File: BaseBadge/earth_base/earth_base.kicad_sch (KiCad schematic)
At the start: 8 parts, among them J1 Conn_02x03_Counter_Clockwise, J2 Conn_02x03_Counter_Clockwise

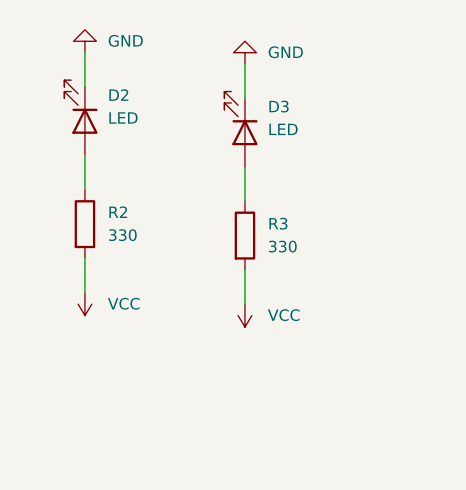
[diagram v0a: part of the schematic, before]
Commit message: overhauls across boards to v02
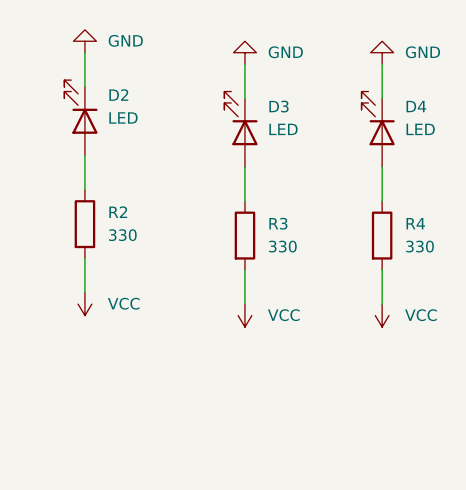
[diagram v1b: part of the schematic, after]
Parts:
- added D4: LED, LED_SMD:LED_1206_3216Metric_Pad1.42x1.75mm_HandSolder, symbol Device:LED
- added R4: 330, Resistor_SMD:R_1206_3216Metric, symbol Device:R
- D1, D2, D3: footprint (none) -> LED_SMD:LED_1206_3216Metric_Pad1.42x1.75mm_HandSolder
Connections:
- net GND: now also D4.1 (K)
- net VCC: now also R4.2
- new net: D4.2 (A), R4.1
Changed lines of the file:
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@@
+    (stroke (width 0) (type default) (color 0 0 0 0))
+  )
+  (wire (pts (xy 208.28 64.77) (xy 208.28 68.58))
     (stroke (width 0) (type default) (color 0 0 0 0))
   )
@@
     (stroke (width 0) (type default) (color 0 0 0 0))
   )
+  (wire (pts (xy 208.28 76.2) (xy 208.28 80.01))
+    (stroke (width 0) (type default) (color 0 0 0 0))
+  )
   (wire (pts (xy 128.27 143.51) (xy 163.83 143.51))
     (stroke (width 0) (type default) (color 0 0 0 0))
@@
     (stroke (width 0) (type default) (color 0 0 0 0))
   )
+  (wire (pts (xy 208.28 87.63) (xy 208.28 91.44))
+    (stroke (width 0) (type default) (color 0 0 0 0))
+  )
   (wire (pts (xy 128.27 127) (xy 128.27 143.51))
     (stroke (width 0) (type default) (color 0 0 0 0))
@@
   (wire (pts (xy 123.19 132.08) (xy 123.19 138.43))
     (stroke (width 0) (type default) (color 0 0 0 0))
+  )
+  (symbol (lib_id "power:VCC") (at 208.28 91.44 180) (unit 1)
+    (in_bom yes) (on_board yes) (fields_autoplaced)
+    (property "Reference" "#PWR012" (id 0) (at 208.28 87.63 0)
+      (effects (font (size 1.27 1.27)) hide)
+    )
+    (property "Value" "VCC" (id 1) (at 210.82 92.7099 0)
+      (effects (font (size 1.27 1.27)) (justify right))
+    )
+    (property "Footprint" "" (id 2) (at 208.28 91.44 0)
+      (effects (font (size 1.27 1.27)) hide)
+    )
+    (property "Datasheet" "" (id 3) (at 208.28 91.44 0)
+      (effects (font (size 1.27 1.27)) hide)
+    )
+    (pin "1")
   )
   (symbol (lib_id "power:PWR_FLAG") (at 110.49 127 0) (unit 1)
@@
       (effects (font (size 1.27 1.27)) (justify left))
     )
-    (property "Footprint" "" (id 2) (at 175.26 71.12 0)
+    (property "Footprint" "LED_SMD:LED_1206_3216Metric_Pad1.42x1.75mm_HandSolder" (id 2) (at 175.26 71.12 0)
       (effects (font (size 1.27 1.27)) hide)
     )
@@
     )
     (pin "1")
+  )
+  (symbol (lib_id "Device:LED") (at 208.28 72.39 270) (unit 1)
+    (in_bom yes) (on_board yes)
+    (property "Reference" "D4" (id 0) (at 210.82 69.5324 90)
+      (effects (font (size 1.27 1.27)) (justify left))
+    )
+    (property "Value" "LED" (id 1) (at 210.82 72.0724 90)
+      (effects (font (size 1.27 1.27)) (justify left))
+    )
+    (property "Footprint" "LED_SMD:LED_1206_3216Metric_Pad1.42x1.75mm_HandSolder" (id 2) (at 208.28 72.39 0)
+      (effects (font (size 1.27 1.27)) hide)
+    )
+    (property "Datasheet" "~" (id 3) (at 208.28 72.39 0)
+      (effects (font (size 1.27 1.27)) hide)
+    )
+    (pin "1")
+    (pin "2")
   )
   (symbol (lib_id "power:PWR_FLAG") (at 146.05 127 0) (unit 1)
@@
     )
     (pin "1")
+  )
+  (symbol (lib_id "Device:R") (at 208.28 83.82 0) (unit 1)
+    (in_bom yes) (on_board yes) (fields_autoplaced)
+    (property "Reference" "R4" (id 0) (at 210.82 82.5499 0)
+      (effects (font (size 1.27 1.27)) (justify left))
+    )
+    (property "Value" "330" (id 1) (at 210.82 85.0899 0)
+      (effects (font (size 1.27 1.27)) (justify left))
+    )
+    (property "Footprint" "Resistor_SMD:R_1206_3216Metric" (id 2) (at 206.502 83.82 90)
+      (effects (font (size 1.27 1.27)) hide)
+    )
+    (property "Datasheet" "~" (id 3) (at 208.28 83.82 0)
+      (effects (font (size 1.27 1.27)) hide)
+    )
+    (pin "1")
+    (pin "2")
   )
   (symbol (lib_id "power:GND") (at 193.04 64.77 180) (unit 1)
@@
       (effects (font (size 1.27 1.27)) (justify left))
     )
-    (property "Footprint" "" (id 2) (at 158.75 69.85 0)
+    (property "Footprint" "LED_SMD:LED_1206_3216Metric_Pad1.42x1.75mm_HandSolder" (id 2) (at 158.75 69.85 0)
       (effects (font (size 1.27 1.27)) hide)
     )
@@
       (effects (font (size 1.27 1.27)) (justify left))
     )
-    (property "Footprint" "" (id 2) (at 193.04 72.39 0)
+    (property "Footprint" "LED_SMD:LED_1206_3216Metric_Pad1.42x1.75mm_HandSolder" (id 2) (at 193.04 72.39 0)
       (effects (font (size 1.27 1.27)) hide)
     )
@@
     (pin "1")
     (pin "2")
+  )
+  (symbol (lib_id "power:GND") (at 208.28 64.77 180) (unit 1)
+    (in_bom yes) (on_board yes) (fields_autoplaced)
+    (property "Reference" "#PWR011" (id 0) (at 208.28 58.42 0)
+      (effects (font (size 1.27 1.27)) hide)
+    )
+    (property "Value" "GND" (id 1) (at 210.82 63.4999 0)
+      (effects (font (size 1.27 1.27)) (justify right))
+    )
+    (property "Footprint" "" (id 2) (at 208.28 64.77 0)
+      (effects (font (size 1.27 1.27)) hide)
+    )
+    (property "Datasheet" "" (id 3) (at 208.28 64.77 0)
+      (effects (font (size 1.27 1.27)) hide)
+    )
+    (pin "1")
   )
   (symbol (lib_id "power:VCC") (at 175.26 90.17 180) (unit 1)
@@
       (reference "#PWR010") (unit 1) (value "VCC") (footprint "")
     )
+    (path "/7d7486ae-aeaa-4bbe-ab12-2142f8812c98"
+      (reference "#PWR011") (unit 1) (value "GND") (footprint "")
+    )
+    (path "/00fd3b26-9e35-452b-b74a-ccc9e0f65386"
+      (reference "#PWR012") (unit 1) (value "VCC") (footprint "")
+    )
     (path "/6ad5c8e3-405d-4457-b239-10abb6e3be61"
       (reference "D1") (unit 1) (value "LED") (footprint "LED_SMD:LED_1206_3216Metric_Pad1.42x1.75mm_HandSolder")
@@
       (reference "D3") (unit 1) (value "LED") (footprint "LED_SMD:LED_1206_3216Metric_Pad1.42x1.75mm_HandSolder")
     )
+    (path "/25b042b4-fb53-4dfb-be34-9dd5a92f841c"
+      (reference "D4") (unit 1) (value "LED") (footprint "LED_SMD:LED_1206_3216Metric_Pad1.42x1.75mm_HandSolder")
+    )
     (path "/6995beeb-7854-4705-ae35-78174cb5e8c5"
       (reference "J1") (unit 1) (value "Conn_02x03_Counter_Clockwise") (footprint "Base_Library:sky2ground_connector")
@@
       (reference "R3") (unit 1) (value "330") (footprint "Resistor_SMD:R_1206_3216Metric")
     )
-  )
+    (path "/444cd72f-762b-46a7-ba6e-42378802e873"
+      (reference "R4") (unit 1) (value "330") (footprint "Resistor_SMD:R_1206_3216Metric")
+    )
+  )

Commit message: updated earth portion for fabrication
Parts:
- D1, D2, D3, D4: footprint LED_SMD:LED_1206_3216Metric_Pad1.42x1.75mm_HandSolder -> (none)
- R1, R2, R3, R4: footprint Resistor_SMD:R_1206_3216Metric -> Resistor_SMD:R_0805_2012Metric
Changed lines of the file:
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@@
       (effects (font (size 1.27 1.27)) (justify left))
     )
-    (property "Footprint" "LED_SMD:LED_1206_3216Metric_Pad1.42x1.75mm_HandSolder" (id 2) (at 175.26 71.12 0)
+    (property "Footprint" "" (id 2) (at 175.26 71.12 0)
       (effects (font (size 1.27 1.27)) hide)
     )
@@
       (effects (font (size 1.27 1.27)) (justify left))
     )
-    (property "Footprint" "LED_SMD:LED_1206_3216Metric_Pad1.42x1.75mm_HandSolder" (id 2) (at 208.28 72.39 0)
+    (property "Footprint" "" (id 2) (at 208.28 72.39 0)
       (effects (font (size 1.27 1.27)) hide)
     )
@@
       (effects (font (size 1.27 1.27)) (justify left))
     )
-    (property "Footprint" "Resistor_SMD:R_1206_3216Metric" (id 2) (at 206.502 83.82 90)
+    (property "Footprint" "Resistor_SMD:R_0805_2012Metric" (id 2) (at 206.502 83.82 90)
       (effects (font (size 1.27 1.27)) hide)
     )
@@
       (effects (font (size 1.27 1.27)) (justify left))
     )
-    (property "Footprint" "Resistor_SMD:R_1206_3216Metric" (id 2) (at 191.262 83.82 90)
+    (property "Footprint" "Resistor_SMD:R_0805_2012Metric" (id 2) (at 191.262 83.82 90)
       (effects (font (size 1.27 1.27)) hide)
     )
@@
       (effects (font (size 1.27 1.27)) (justify left))
     )
-    (property "Footprint" "LED_SMD:LED_1206_3216Metric_Pad1.42x1.75mm_HandSolder" (id 2) (at 158.75 69.85 0)
+    (property "Footprint" "" (id 2) (at 158.75 69.85 0)
       (effects (font (size 1.27 1.27)) hide)
     )
@@
       (effects (font (size 1.27 1.27)) (justify left))
     )
-    (property "Footprint" "LED_SMD:LED_1206_3216Metric_Pad1.42x1.75mm_HandSolder" (id 2) (at 193.04 72.39 0)
+    (property "Footprint" "" (id 2) (at 193.04 72.39 0)
       (effects (font (size 1.27 1.27)) hide)
     )
@@
       (effects (font (size 1.27 1.27)) (justify left))
     )
-    (property "Footprint" "Resistor_SMD:R_1206_3216Metric" (id 2) (at 156.972 81.28 90)
+    (property "Footprint" "Resistor_SMD:R_0805_2012Metric" (id 2) (at 156.972 81.28 90)
       (effects (font (size 1.27 1.27)) hide)
     )
@@
       (effects (font (size 1.27 1.27)) (justify left))
     )
-    (property "Footprint" "Resistor_SMD:R_1206_3216Metric" (id 2) (at 173.482 82.55 90)
+    (property "Footprint" "Resistor_SMD:R_0805_2012Metric" (id 2) (at 173.482 82.55 90)
       (effects (font (size 1.27 1.27)) hide)
     )
@@
     )
     (path "/6ad5c8e3-405d-4457-b239-10abb6e3be61"
-      (reference "D1") (unit 1) (value "LED") (footprint "LED_SMD:LED_1206_3216Metric_Pad1.42x1.75mm_HandSolder")
+      (reference "D1") (unit 1) (value "LED") (footprint "Base_Library:19-213_Y2C-CO2R2L_3T(CY)")
     )
     (path "/20095479-8387-4c2a-81af-72dd0a3c8d74"
-      (reference "D2") (unit 1) (value "LED") (footprint "LED_SMD:LED_1206_3216Metric_Pad1.42x1.75mm_HandSolder")
+      (reference "D2") (unit 1) (value "LED") (footprint "Base_Library:19-213_Y2C-CO2R2L_3T(CY)")
     )
     (path "/6d713df6-86c3-4714-b3aa-4d0895fe5cf0"
-      (reference "D3") (unit 1) (value "LED") (footprint "LED_SMD:LED_1206_3216Metric_Pad1.42x1.75mm_HandSolder")
+      (reference "D3") (unit 1) (value "LED") (footprint "Base_Library:19-213_Y2C-CO2R2L_3T(CY)")
     )
     (path "/25b042b4-fb53-4dfb-be34-9dd5a92f841c"
-      (reference "D4") (unit 1) (value "LED") (footprint "LED_SMD:LED_1206_3216Metric_Pad1.42x1.75mm_HandSolder")
+      (reference "D4") (unit 1) (value "LED") (footprint "Base_Library:19-213_Y2C-CO2R2L_3T(CY)")
     )
     (path "/6995beeb-7854-4705-ae35-78174cb5e8c5"
@@
     )
     (path "/c50735f4-6020-400c-a452-2ae81a0d9fc9"
-      (reference "R1") (unit 1) (value "330") (footprint "Resistor_SMD:R_1206_3216Metric")
+      (reference "R1") (unit 1) (value "330") (footprint "Resistor_SMD:R_0805_2012Metric")
     )
     (path "/c5bc07f9-8446-40c9-87a9-a34ee819a5e6"
-      (reference "R2") (unit 1) (value "330") (footprint "Resistor_SMD:R_1206_3216Metric")
+      (reference "R2") (unit 1) (value "330") (footprint "Resistor_SMD:R_0805_2012Metric")
     )
     (path "/5da077d7-42aa-4023-ad05-49eb1660bcbd"
-      (reference "R3") (unit 1) (value "330") (footprint "Resistor_SMD:R_1206_3216Metric")
+      (reference "R3") (unit 1) (value "330") (footprint "Resistor_SMD:R_0805_2012Metric")
     )
     (path "/444cd72f-762b-46a7-ba6e-42378802e873"
-      (reference "R4") (unit 1) (value "330") (footprint "Resistor_SMD:R_1206_3216Metric")
-    )
-  )
+      (reference "R4") (unit 1) (value "330") (footprint "Resistor_SMD:R_0805_2012Metric")
+    )
+  )
